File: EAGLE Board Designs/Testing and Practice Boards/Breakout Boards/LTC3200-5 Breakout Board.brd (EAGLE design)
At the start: 100 x 66 mm, 26 parts, among them J1 JUMPER_1X02_, U1 OPAMP_1_CHANNEL_OPA991, U17 OPAMP_1_CHANNEL_OPA991, U2 OPAMP_1_CHANNEL_OPA991, U3 OPAMP_1_CHANNEL_OPA991

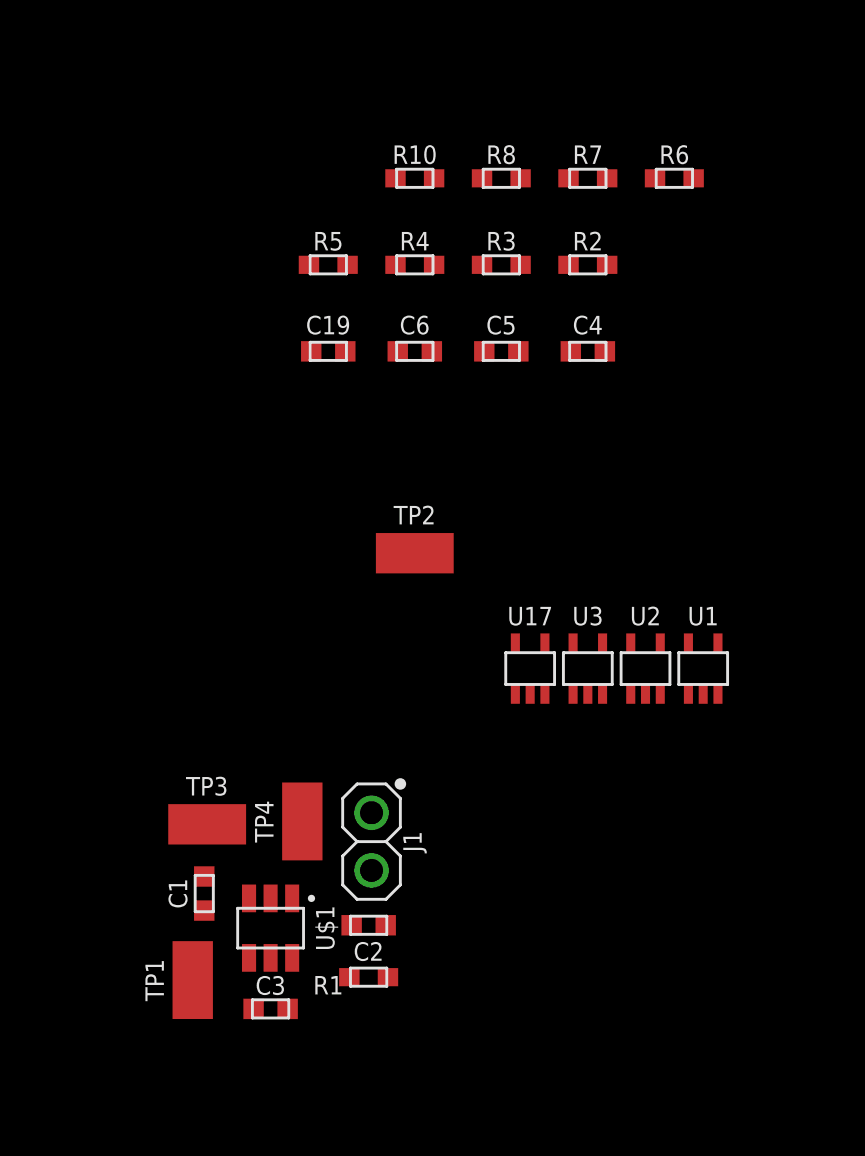
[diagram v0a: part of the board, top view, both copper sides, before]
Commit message: Did most of the traces, having some issues with passing on-campus DRC
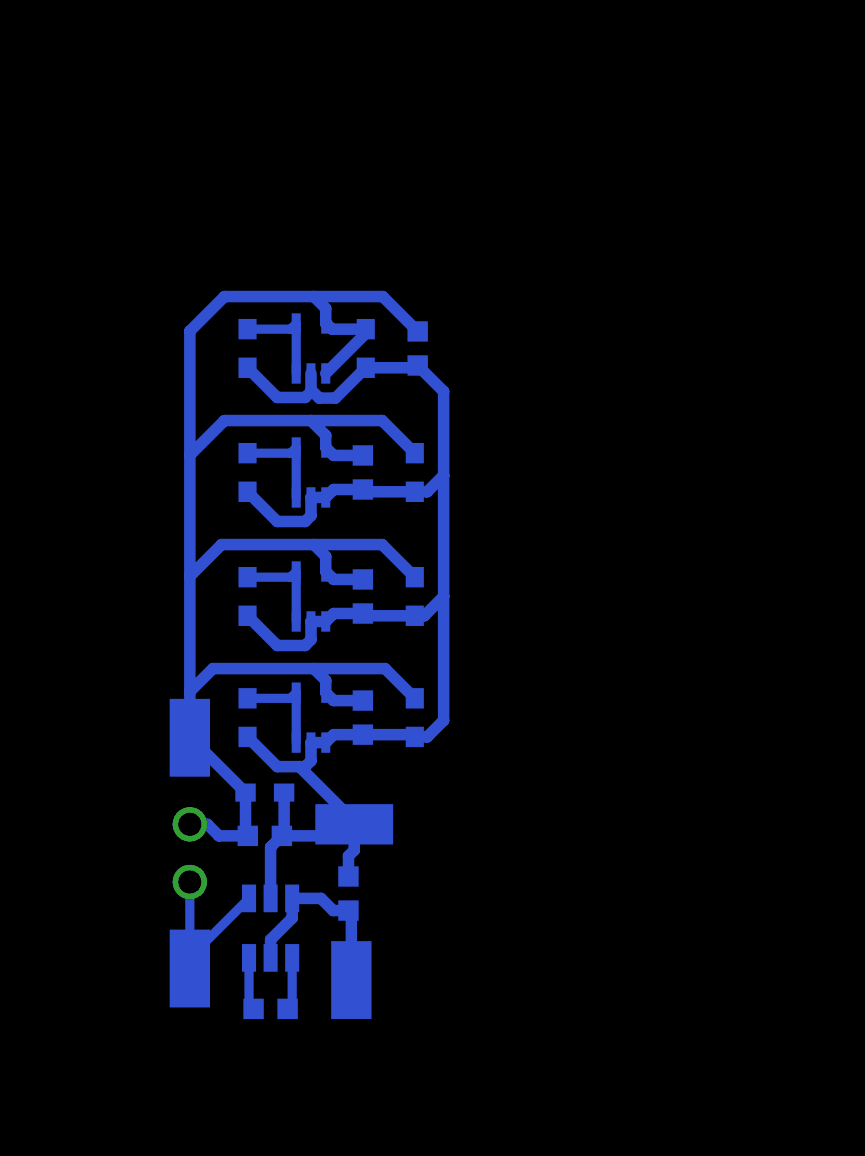
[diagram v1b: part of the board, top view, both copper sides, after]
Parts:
- moved R2 24.9 mm to (11.7, 33.4), flipped to the bottom, turned to 90 degrees
- moved R10 23.7 mm to (19.1, 33.4), flipped to the bottom, turned to 90 degrees
- moved R6 22.8 mm to (11.7, 44.2), flipped to the bottom, turned to 90 degrees
- moved U3 18.6 mm to (14.5, 49.7), flipped to the bottom
- moved U1 17.6 mm to (14.5, 38.7), flipped to the bottom
- moved U2 17.1 mm to (14.5, 44.2), flipped to the bottom
- moved R4 16.4 mm to (11.7, 38.7), flipped to the bottom, turned to 90 degrees
- moved C19 16.2 mm to (16.8, 33.4), flipped to the bottom, turned to 270 degrees
- moved R3 15.1 mm to (19.1, 38.7), flipped to the bottom, turned to 90 degrees
- moved C4 14.7 mm to (16.8, 38.7), flipped to the bottom, turned to 270 degrees
- moved R8 13.5 mm to (11.7, 49.7), flipped to the bottom, turned to 90 degrees
- moved TP2 12.8 mm to (9.14, 32.5), flipped to the bottom, turned to 90 degrees
- moved R7 12.3 mm to (16.9, 49.7), flipped to the bottom, turned to 90 degrees
- moved R5 9.91 mm to (19.1, 44.2), flipped to the bottom, turned to 90 degrees
- moved U17 9.89 mm to (14.5, 33.4), flipped to the bottom
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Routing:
- net +5V: track 0.00 -> 85.9 mm
- net GND: track 0.00 -> 71.8 mm
- net BRAKE1_BUFF_5V: track 0.00 -> 17.8 mm
- net +3V3: track 0.00 -> 8.83 mm
- net 5V_PRE: track 0.00 -> 7.98 mm
- net N$4: track 0.00 -> 2.33 mm
- net N$3: track 0.00 -> 2.33 mm

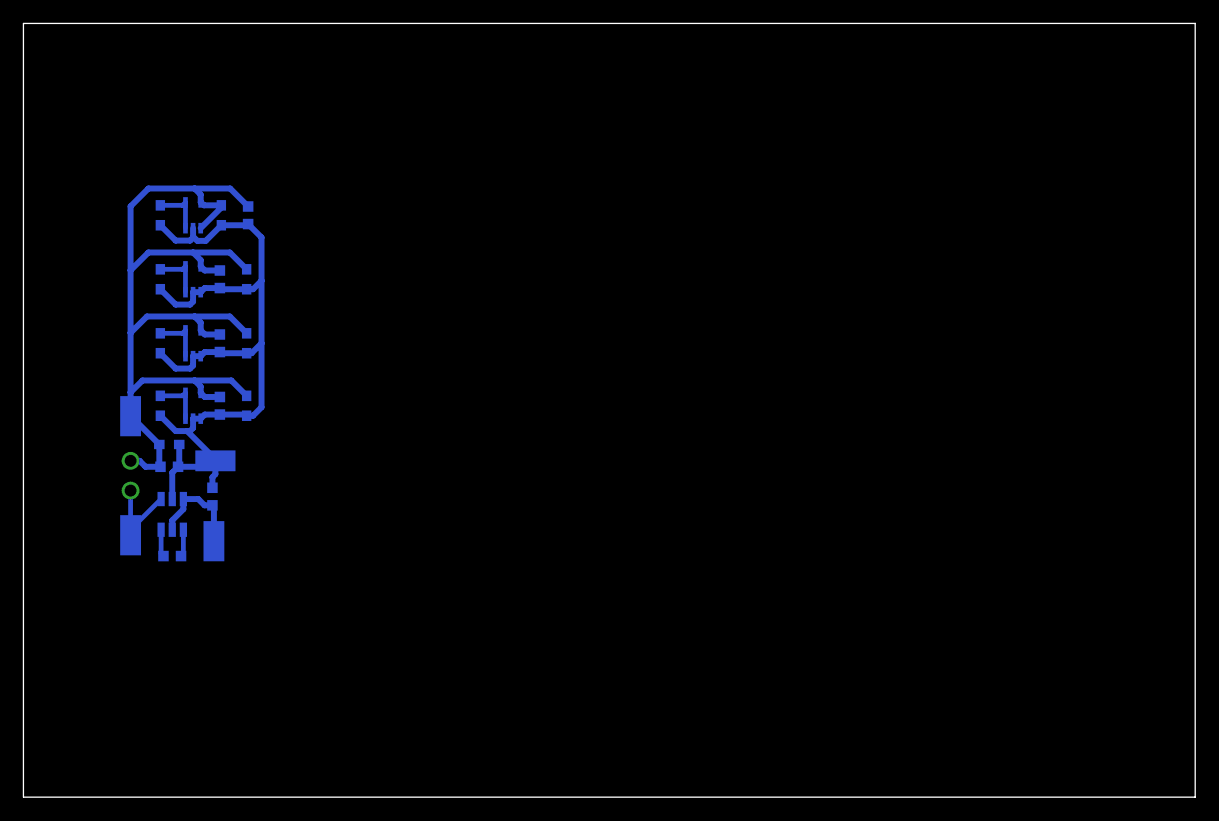
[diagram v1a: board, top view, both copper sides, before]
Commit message: Finished all traces on board, still yet to pass DRC
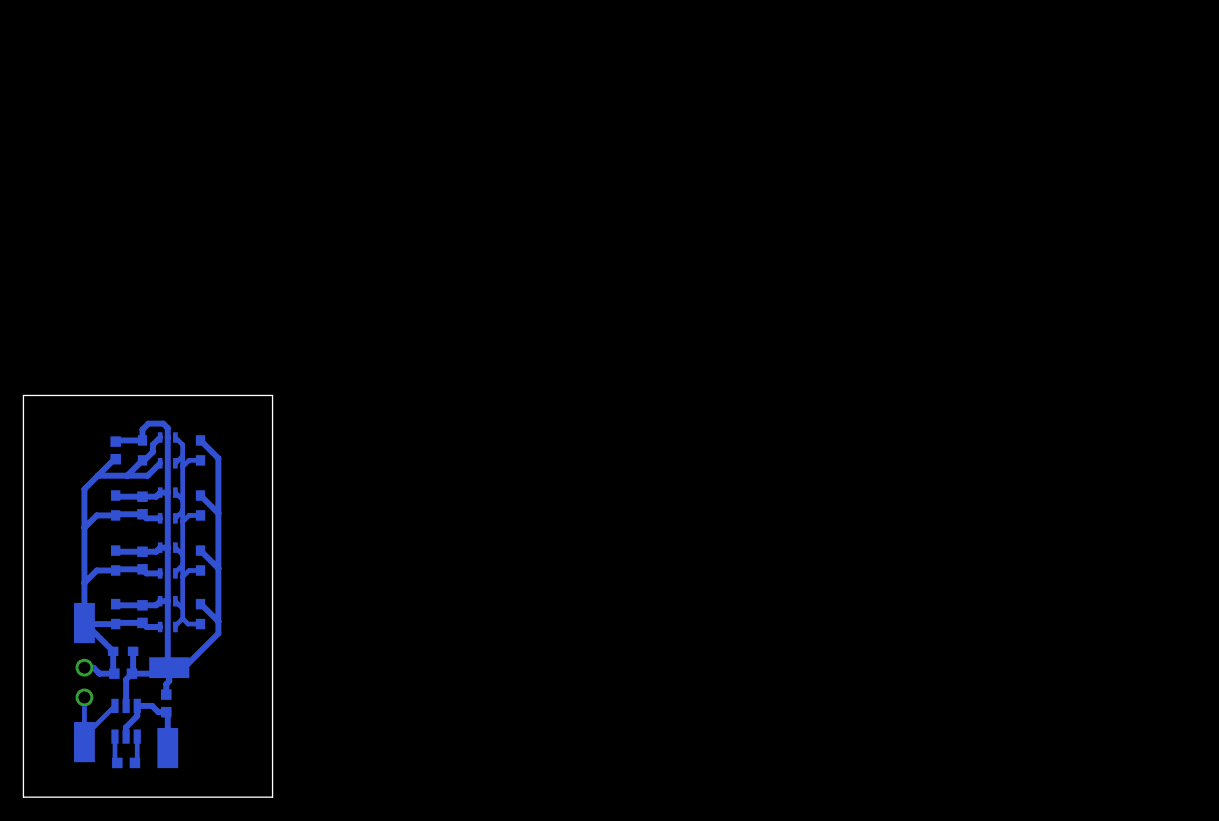
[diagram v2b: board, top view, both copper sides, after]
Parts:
- moved C6 23.0 mm to (7.87, 29.6), turned to 90 degrees
- moved R5 22.3 mm to (7.87, 24.9), turned to 270 degrees
- moved R3 21.6 mm to (7.87, 20.2), turned to 270 degrees
- moved R7 21.2 mm to (10.2, 29.6), turned to 270 degrees
- moved R10 21.0 mm to (7.87, 15.6), turned to 270 degrees
- moved C5 20.4 mm to (10.2, 24.9), turned to 90 degrees
- moved R8 20.4 mm to (15.1, 29.6), turned to 270 degrees
- moved U3 20.2 mm to (12.3, 29.6), turned to 180 degrees
- moved C4 19.7 mm to (10.2, 20.2), turned to 90 degrees
- moved R6 19.6 mm to (15.1, 24.9), turned to 270 degrees
- moved U2 19.4 mm to (12.3, 24.9), turned to 180 degrees
- moved C19 19.0 mm to (10.2, 15.6), turned to 90 degrees
- moved R4 18.9 mm to (15.1, 20.2), turned to 270 degrees
- moved U1 18.7 mm to (12.3, 20.2), turned to 180 degrees
- moved R2 18.1 mm to (15.1, 15.6), turned to 270 degrees
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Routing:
- net +5V: track 85.9 -> 54.5 mm
- net BRAKE1_BUFF_5V: track 17.8 -> 29.0 mm
- net GND: track 71.8 -> 79.8 mm
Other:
- board size 100 x 66 mm -> 21.3 x 34.3 mm
